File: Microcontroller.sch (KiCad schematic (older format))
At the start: 6 parts, among them J13 640456-3, J14 640456-3, J15 640456-3, J16 B5B-XH-A_LF__SN_, J17 0022232041, U11 STM32H743ZIT6

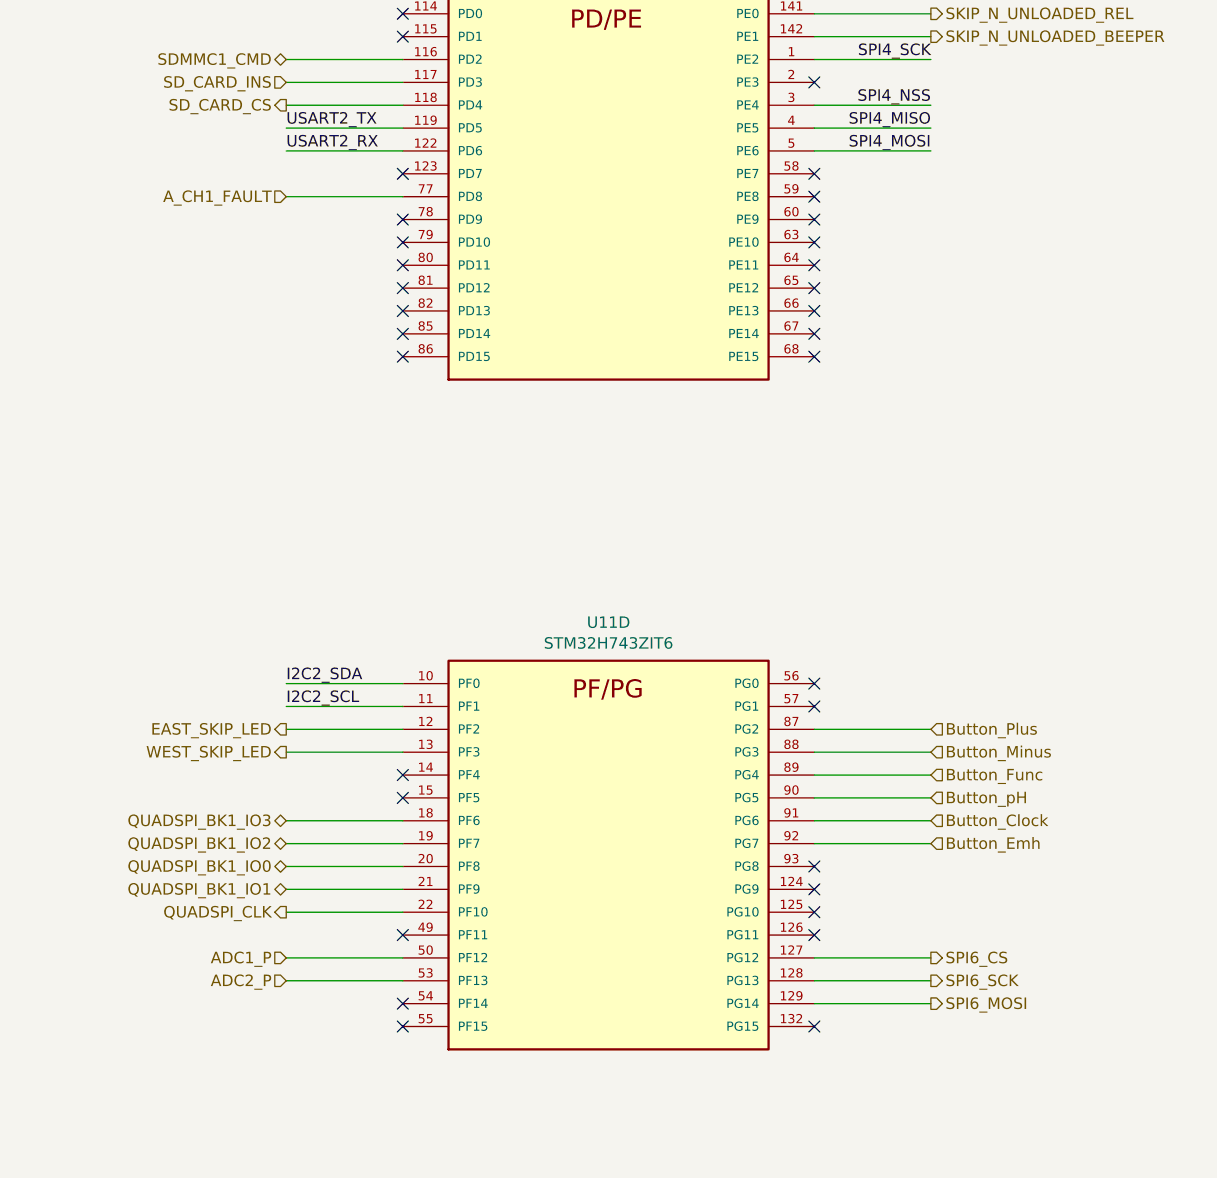
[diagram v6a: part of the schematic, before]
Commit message: SPI6 changed to SPI1
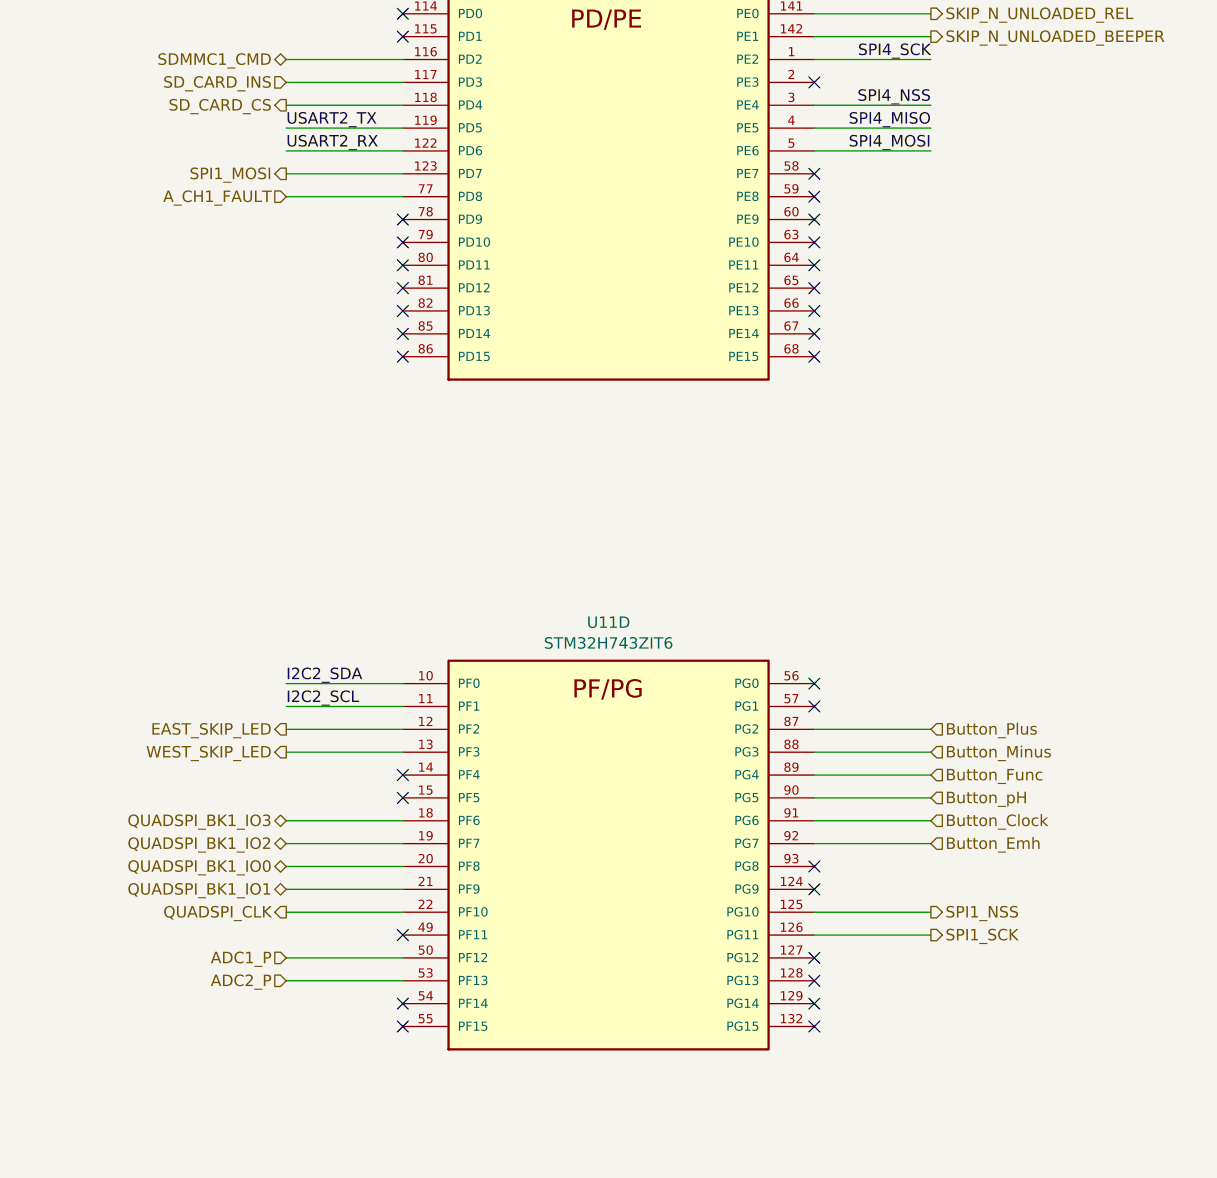
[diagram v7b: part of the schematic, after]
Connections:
- net SPI1_MOSI: now reaches U11.123 (PD7)
- net SPI1_NSS: now reaches U11.125 (PG10)
- net SPI1_SCK: now reaches U11.126 (PG11)
- net SPI6_CS: no longer names the net of U11.127 (PG12)
- net SPI6_MOSI: no longer names the net of U11.129 (PG14)
- net SPI6_SCK: no longer names the net of U11.128 (PG13)
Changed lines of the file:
@@
 Text Label 6130 1910 0    50   ~ 0
 USART2_RX
-NoConn ~ 6640 2010
 Text HLabel 1270 2810 0    50   Input ~ 0
 LEVEL_SWITCH
@@
 Button_Func
 Wire Wire Line
-	8440 5440 8950 5440
-Text HLabel 8950 5440 2    50   Output ~ 0
-SPI6_CS
+	8440 5240 8950 5240
+Text HLabel 8950 5240 2    50   Output ~ 0
+SPI1_NSS
 NoConn ~ 8440 5140
-NoConn ~ 8440 5240
-NoConn ~ 8440 5340
-Wire Wire Line
-	8440 5540 8950 5540
-Text HLabel 8950 5540 2    50   Output ~ 0
-SPI6_SCK
-Wire Wire Line
-	8440 5640 8950 5640
-Text HLabel 8950 5640 2    50   Output ~ 0
-SPI6_MOSI
+Wire Wire Line
+	8440 5340 8950 5340
+Text HLabel 8950 5340 2    50   Output ~ 0
+SPI1_SCK
+Text HLabel 6130 2010 0    50   Output ~ 0
+SPI1_MOSI
 NoConn ~ 8440 5040
 NoConn ~ 8440 5740
@@
 Wire Wire Line
 	1650 6430 1750 6430
+Wire Wire Line
+	6130 2010 6640 2010
+NoConn ~ 8440 5640
+NoConn ~ 8440 5540
+NoConn ~ 8440 5440
 $EndSCHEMATC

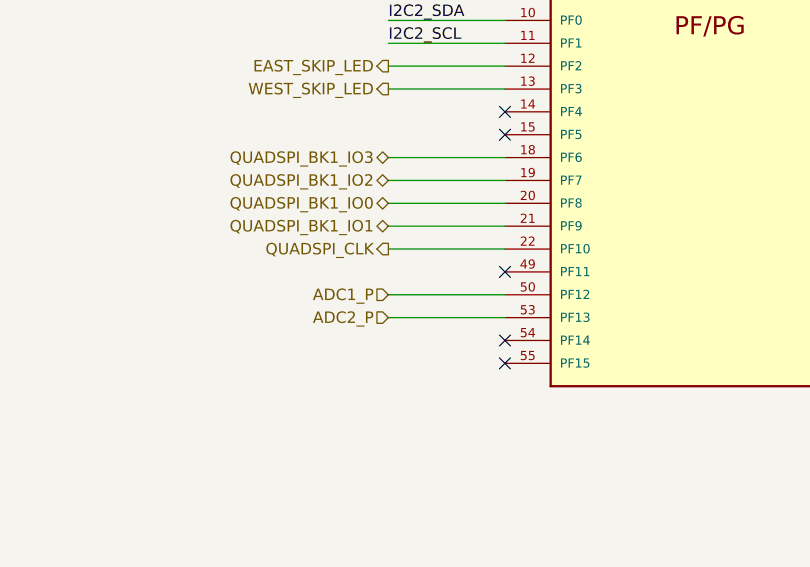
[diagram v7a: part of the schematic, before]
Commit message: ADC1 input changed from IN6 to IN2
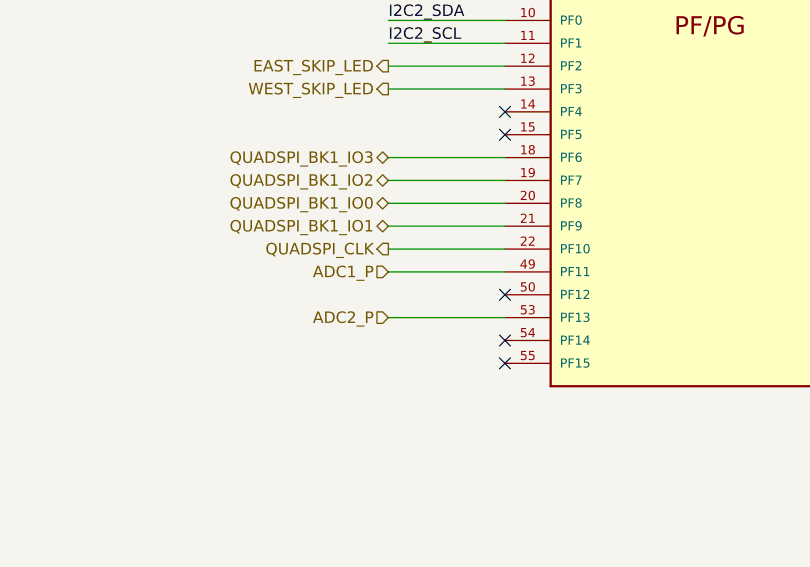
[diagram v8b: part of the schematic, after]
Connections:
- net ADC1_P: now also U11.49 (PF11); no longer U11.50 (PF12)
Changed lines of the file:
@@
 Wire Wire Line
 	6130 2110 6640 2110
-Text HLabel 6130 5440 0    50   Input ~ 0
+Text HLabel 6130 5340 0    50   Input ~ 0
 ADC1_P
-Wire Wire Line
-	6130 5440 6640 5440
 Text HLabel 6130 5540 0    50   Input ~ 0
 ADC2_P
@@
 NoConn ~ 6640 2210
 NoConn ~ 6640 5640
-NoConn ~ 6640 5340
 NoConn ~ 6640 4640
 $Comp
@@
 NoConn ~ 8440 5540
 NoConn ~ 8440 5440
+Wire Wire Line
+	6130 5340 6640 5340
+NoConn ~ 6640 5440
 $EndSCHEMATC
